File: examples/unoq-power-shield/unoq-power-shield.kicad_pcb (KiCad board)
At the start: 4 copper layers, 53.3 x 68.6 mm, 56 parts, among them J1 VIN 7-24V, J10 UNO PWR, J11 UNO ANALOG, J12 UNO D0-D7, J13 UNO D8-SCL, J2 5V OUT, J3 Qwiic, J4 Qwiic, J5 5V IO, Q1 BSS138LT1G, Q2 BSS138LT1G, Q3 BSS138LT1G, Q4 BSS138LT1G, Q5 AO4407A, U1 TPS54331DDAR, U2 INA226AIDGSR

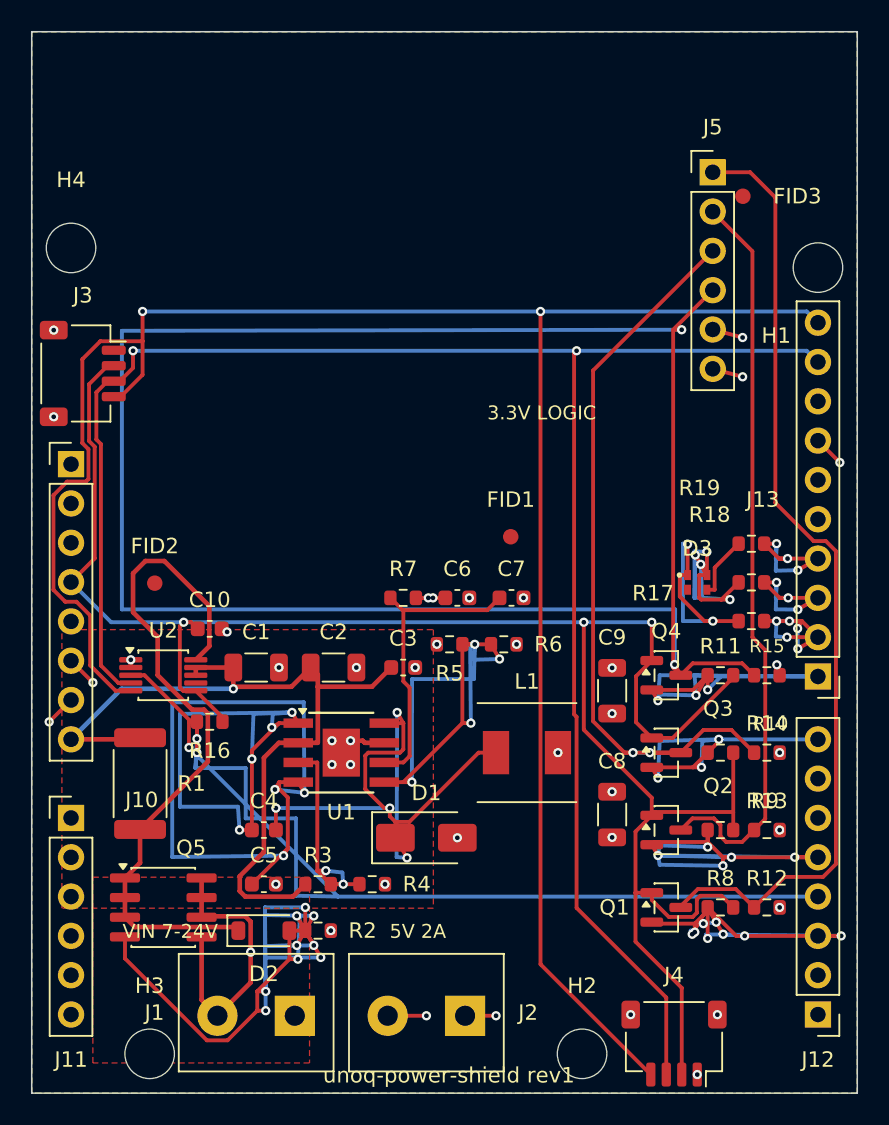
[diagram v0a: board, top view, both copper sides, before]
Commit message: Example board signed off pre-order; add the your-own-board walkthrough
Example (unoq-power-shield), placement/routing rounds to sign-off:
- Final state: 0 unconnected and 0 clearance violations across 5
  identical DRC runs; checker 14 passed / 0 failed; ERC clean; all 24
  JLC BOM lines verified in stock. The 17 residual DRC items (3 kinds)
  are each explained in rev-1-plan.md's new ledger - Qwiic edge pads,
  UNO form-factor header/hole adjacency, courtyard grazes.
- The two structural fixes that ended the recurring PH-past-FB
  clearance cluster: the VIN pour now stops LEFT of U1's pad column
  (as fixed DSN copper it walled off the east corridor and forced PH
  under the chip), and the FB divider + COMP network moved from north
  (y=31-34) to a topology-ordered row south of U1 - FB drops straight
  onto R6/R5 from pin 5, COMP hooks east around the corner onto R7/C7,
  rotations chosen so each pad's net faces its incoming track.
- U2 (MSOP-10) fanout: fan out ONLY pad 7 (GND, plane-fed) via
  skip_pads. A full fanout of a 0.5 mm-pitch part self-blocks: each
  ring via sits one pad pitch from its neighbour's stub, inside the
  0.15 mm clearance at any legal via size (min via 0.5 + min track
  0.2 lands exactly on the pass-a-neighbour bound, and equality
  fails). Alone, the one via that matters fits. Rationale in
  board.toml.
- D3's 5V pad was a dead island (no same-net surface neighbour):
  bonded with a concentric thermal via to the In2 plane.
- Clearance regime settled: netclass clearance IS the DRC constraint
  (0.15 - the MSOP's own 0.2 mm pad gaps must not self-flag);
  completion/astar at 0.16; export_dsn bumps DSN clearances +10 um so
  routed gaps clear the constraint with margin. apply_netclasses
  re-enforces the class clearance from [route].clearance_mm every run.
- bom.csv: 24 lines, every LCSC code verified in stock 2026-08-30.

Pipeline fixes the example paid for:
- export_dsn: +10 um router margin over the DRC constraint;
  class-name comma sanit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
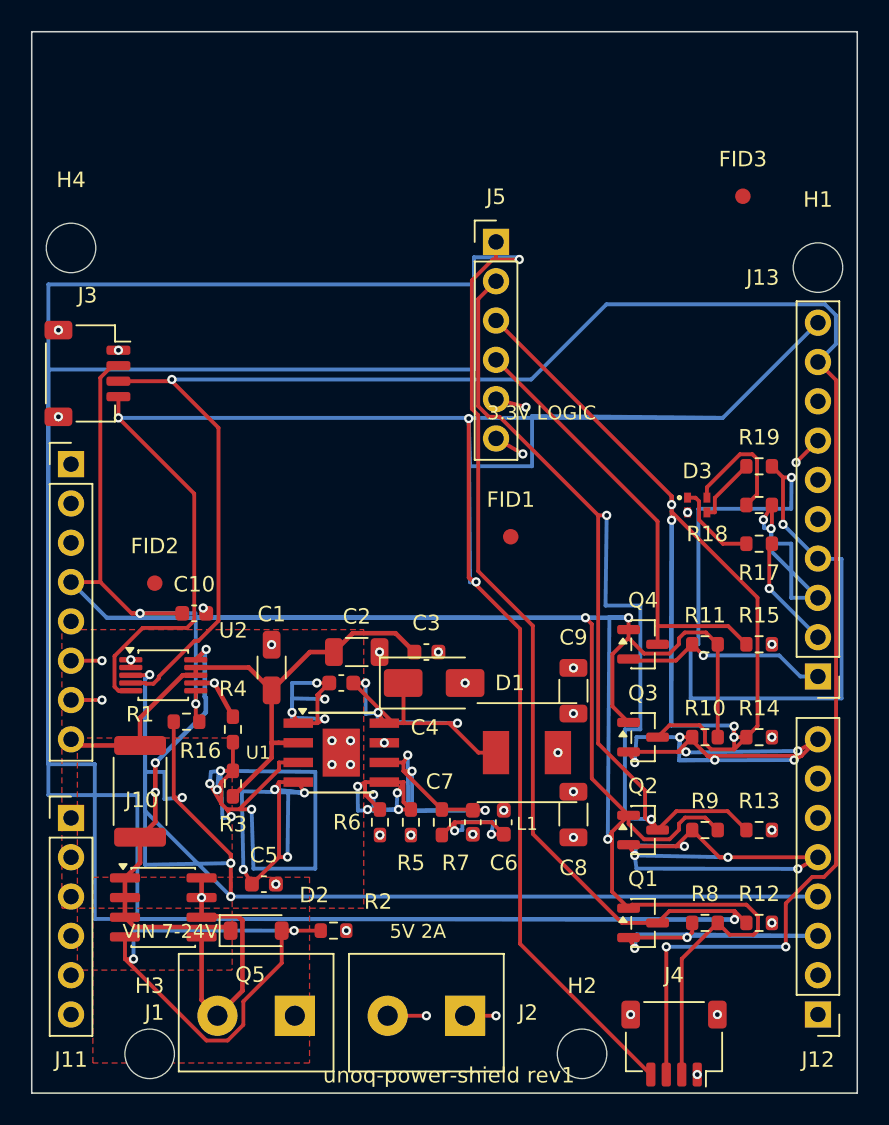
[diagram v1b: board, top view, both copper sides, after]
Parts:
- moved C6 14.8 mm to (152.3, 121.8), turned to 90 degrees
- moved C7 14.7 mm to (150.3, 121.8), turned to -90 degrees
- moved R7 14.7 mm to (148.3, 121.8), turned to -90 degrees
- moved J5 14.7 mm to (151.8, 84.3)
- moved R6 14.0 mm to (144.3, 121.8), turned to -90 degrees
- moved R4 13.5 mm to (134.8, 115.8), turned to 90 degrees
- moved R5 11.8 mm to (146.3, 121.8), turned to 90 degrees
- moved C4 10.7 mm to (141.8, 112.8)
- moved D1 10.0 mm to (147.8, 112.8)
- moved R3 8.51 mm to (134.8, 119.3), turned to 90 degrees
- moved R17 5.02 mm to (168.8, 103.8)
- moved R18 5.02 mm to (168.8, 101.3)
- moved R19 5.02 mm to (168.8, 98.8)
- moved D3 5.00 mm to (164.8, 101.3)
- moved C8 2.50 mm to (156.8, 121.3)
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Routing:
- net HV1: track 62.1 -> 291.8 mm, vias 0 -> 2
- net HV4: track 126.4 -> 28.9 mm, vias 2 -> 0
- net 3V3_UNO: track 130.5 -> 222.6 mm, vias 3 -> 5
- net UNO_D11: track 11.7 -> 48.9 mm, vias 3 -> 2
- net ALERT_3V3: track 75.4 -> 107.1 mm, vias 3 -> 4
- net HV3: track 49.7 -> 78.1 mm, vias 2 -> 4
- net EN: track 14.5 -> 41.7 mm, vias 2 -> 5
- net HV2: track 48.1 -> 73.8 mm, vias 0 -> 2
- net Q5_GATE: track 60.0 -> 34.9 mm, vias 9 -> 2
- net BOOT: track 37.6 -> 15.8 mm
- net SCL_3V3: track 133.4 -> 155.0 mm, vias 2 -> 3
- net LV3: track 21.9 -> 43.3 mm, vias 3 -> 6
- net LV4: track 32.4 -> 13.6 mm, vias 3 -> 1
- net FB: track 37.5 -> 20.3 mm, vias 4 -> 5
- net VIN_PROT: track 44.9 -> 27.7 mm, vias 0 -> 3
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- added copper zone on F.Cu, net VIN_PROT
- removed copper zone on B.Cu, net GND
- removed copper zone on F.Cu, net GND
